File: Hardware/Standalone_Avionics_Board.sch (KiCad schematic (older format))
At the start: 4 parts, among them J1 GPS_Ant, J2 Charges Terminal Block, J3 RF_Ant, J6 3-Pin Molex Power

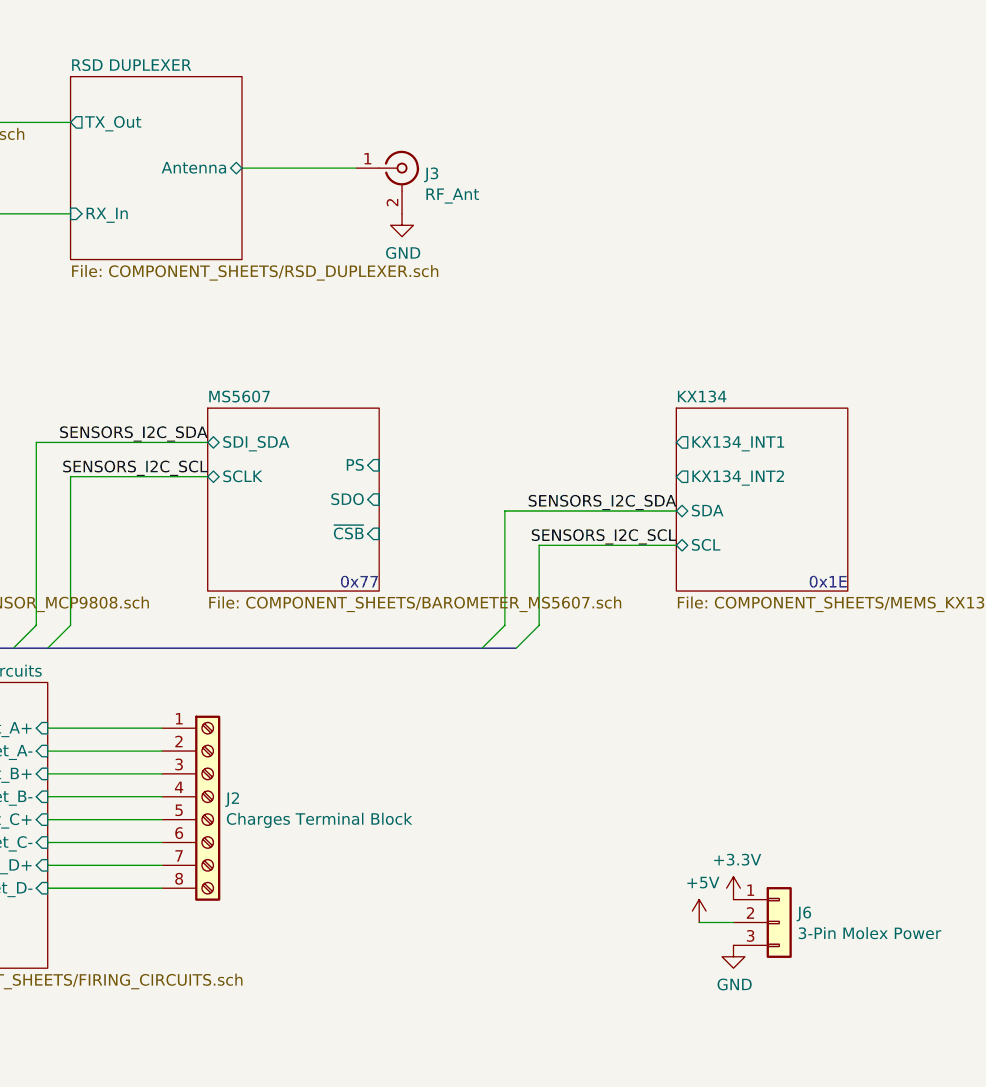
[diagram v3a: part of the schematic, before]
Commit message: Removed microcontroller clock to save space
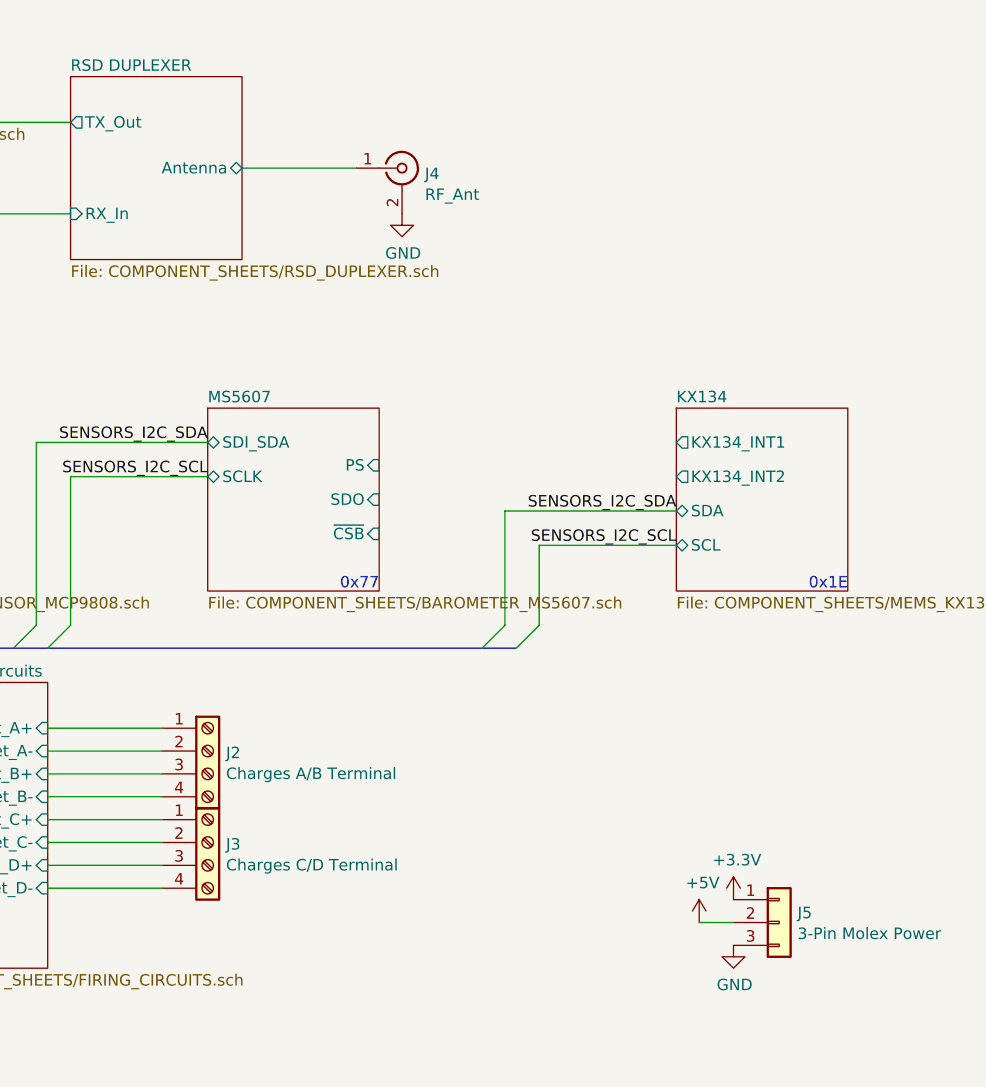
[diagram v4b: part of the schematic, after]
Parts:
- removed J2: Charges Terminal Block, TerminalBlock_Phoenix:TerminalBlock_Phoenix_MKDS-1,5-8-5.08_1x08_P5.08mm_Horizontal, symbol Connector:Screw_Terminal_01x08
- added J2: Charges A/B Terminal, TerminalBlock_Phoenix:TerminalBlock_Phoenix_MKDS-1,5-4_1x04_P5.00mm_Horizontal, symbol Connector:Screw_Terminal_01x04
- added J3: Charges C/D Terminal, TerminalBlock_Phoenix:TerminalBlock_Phoenix_MKDS-1,5-4_1x04_P5.00mm_Horizontal, symbol Connector:Screw_Terminal_01x04
- renumbered J3 to J4, J6 to J5
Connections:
- net Charges Firing Circuits/Fet_A+: now also J2.1 (Pin_1)
- net Charges Firing Circuits/Fet_A-: now also J2.2 (Pin_2)
- net Charges Firing Circuits/Fet_B+: now also J2.3 (Pin_3)
- net Charges Firing Circuits/Fet_B-: now also J2.4 (Pin_4)
- net Charges Firing Circuits/Fet_C+: now also J3.1 (Pin_1)
- net Charges Firing Circuits/Fet_C-: now also J3.2 (Pin_2)
- net Charges Firing Circuits/Fet_D+: now also J3.3 (Pin_3)
- net Charges Firing Circuits/Fet_D-: now also J3.4 (Pin_4)
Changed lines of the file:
@@
 $EndComp
 $Comp
-L Connector:Conn_Coaxial J3
+L Connector:Conn_Coaxial J4
 U 1 1 61B4987D
 P 8300 1700
-F 0 "J3" H 8400 1675 50  0000 L CNN
+F 0 "J4" H 8400 1675 50  0000 L CNN
 F 1 "RF_Ant" H 8400 1584 50  0000 L CNN
 F 2 "Connector_Coaxial:SMA_Amphenol_132134-11_Vertical" H 8300 1700 50  0001 C CNN
@@
 F5 "~CS" I L 3500 5350 50
 $EndSheet
-$Comp
-L Connector:Screw_Terminal_01x08 J2
-U 1 1 61EBDC84
-P 7450 4450
-F 0 "J2" H 7530 4442 50  0000 L CNN
-F 1 "Charges Terminal Block" H 7530 4351 50  0000 L CNN
-F 2 "TerminalBlock_Phoenix:TerminalBlock_Phoenix_MKDS-1,5-8-5.08_1x08_P5.08mm_Horizontal" H 7450 4450 50  0001 C CNN
-F 3 "~" H 7450 4450 50  0001 C CNN
-	1    7450 4450
-	1    0    0    -1
-$EndComp
 $Sheet
 S 5950 3950 800  1250
@@
 	7250 4850 6750 4850
 $Comp
-L power:+3.3V #PWR086
+L power:+3.3V #PWR04
 U 1 1 61B21EEA
 P 9750 4900
-F 0 "#PWR086" H 9750 4750 50  0001 C CNN
+F 0 "#PWR04" H 9750 4750 50  0001 C CNN
 F 1 "+3.3V" H 9765 5073 50  0000 C CNN
 F 2 "" H 9750 4900 50  0001 C CNN
@@
 $EndComp
 $Comp
-L power:GND #PWR087
+L power:GND #PWR05
 U 1 1 61B228F3
 P 9750 5100
-F 0 "#PWR087" H 9750 4850 50  0001 C CNN
+F 0 "#PWR05" H 9750 4850 50  0001 C CNN
 F 1 "GND" H 9755 4927 50  0000 C CNN
 F 2 "" H 9750 5100 50  0001 C CNN
@@
 $EndComp
 $Comp
-L Connector_Generic:Conn_01x03 J6
+L Connector_Generic:Conn_01x03 J5
 U 1 1 61B22E7C
 P 9950 5000
-F 0 "J6" H 10030 5042 50  0000 L CNN
+F 0 "J5" H 10030 5042 50  0000 L CNN
 F 1 "3-Pin Molex Power" H 10030 4951 50  0000 L CNN
 F 2 "Connector_Molex:Molex_KK-254_AE-6410-03A_1x03_P2.54mm_Vertical" H 9950 5000 50  0001 C CNN
@@
 $EndComp
 $Comp
-L power:+5V #PWR085
+L power:+5V #PWR03
 U 1 1 61B248E6
 P 9600 5000
-F 0 "#PWR085" H 9600 4850 50  0001 C CNN
+F 0 "#PWR03" H 9600 4850 50  0001 C CNN
 F 1 "+5V" H 9615 5173 50  0000 C CNN
 F 2 "" H 9600 5000 50  0001 C CNN
@@
 Wire Bus Line
 	2600 3800 8800 3800
+$Comp
+L Connector:Screw_Terminal_01x04 J2
+U 1 1 61B3C495
+P 7450 4250
+F 0 "J2" H 7530 4242 50  0000 L CNN
+F 1 "Charges A/B Terminal" H 7530 4151 50  0000 L CNN
+F 2 "TerminalBlock_Phoenix:TerminalBlock_Phoenix_MKDS-1,5-4_1x04_P5.00mm_Horizontal" H 7450 4250 50  0001 C CNN
+F 3 "~" H 7450 4250 50  0001 C CNN
+	1    7450 4250
+	1    0    0    -1
+$EndComp
+$Comp
+L Connector:Screw_Terminal_01x04 J3
+U 1 1 61B3D949
+P 7450 4650
+F 0 "J3" H 7530 4642 50  0000 L CNN
+F 1 "Charges C/D Terminal" H 7530 4551 50  0000 L CNN
+F 2 "TerminalBlock_Phoenix:TerminalBlock_Phoenix_MKDS-1,5-4_1x04_P5.00mm_Horizontal" H 7450 4650 50  0001 C CNN
+F 3 "~" H 7450 4650 50  0001 C CNN
+	1    7450 4650
+	1    0    0    -1
+$EndComp
 $EndSCHEMATC

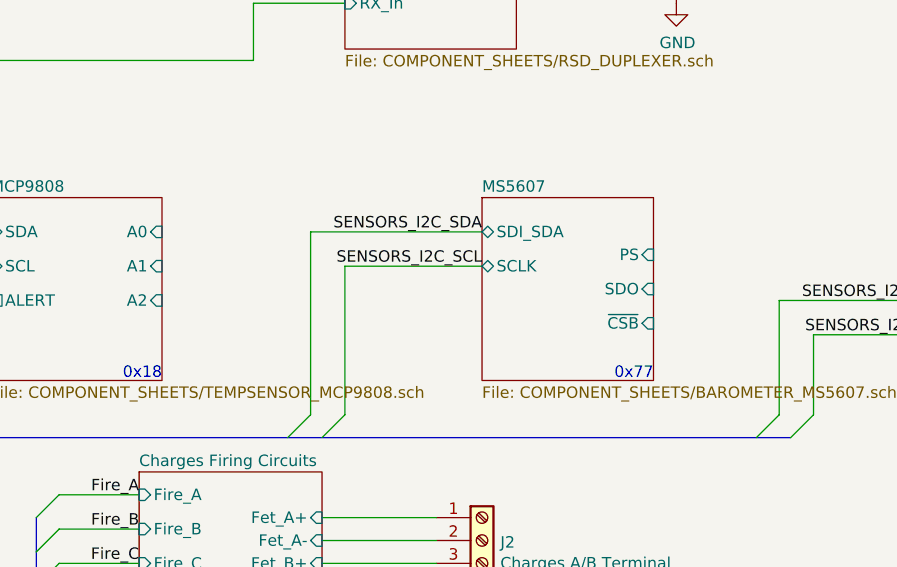
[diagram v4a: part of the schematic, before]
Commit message: Forced addresses for I2C devices
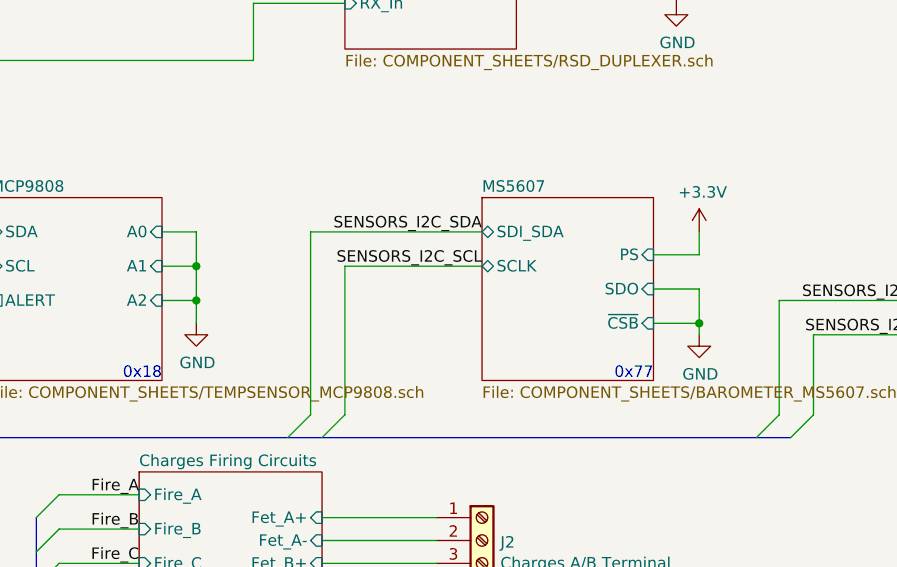
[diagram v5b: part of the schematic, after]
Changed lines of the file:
@@
 Wire Wire Line
 	9750 5000 9600 5000
-Wire Bus Line
-	2600 2900 2600 3800
-Wire Bus Line
-	2350 5850 2350 6500
-Wire Bus Line
-	2350 6500 2950 6500
-Wire Bus Line
-	2350 5500 3100 5500
-Wire Bus Line
-	2350 4850 2350 5500
-Wire Bus Line
-	2250 3500 2250 4550
-Wire Bus Line
-	5500 4150 5500 5200
-Wire Bus Line
-	2600 3800 8800 3800
 $Comp
 L Connector:Screw_Terminal_01x04 J2
@@
 	1    0    0    -1
 $EndComp
+$Comp
+L power:GND #PWR?
+U 1 1 61B8B67C
+P 6200 3300
+F 0 "#PWR?" H 6200 3050 50  0001 C CNN
+F 1 "GND" H 6205 3127 50  0000 C CNN
+F 2 "" H 6200 3300 50  0001 C CNN
+F 3 "" H 6200 3300 50  0001 C CNN
+	1    6200 3300
+	1    0    0    -1
+$EndComp
+Wire Wire Line
+	6200 3300 6200 3200
+Wire Wire Line
+	6200 2900 6050 2900
+Wire Wire Line
+	6050 3050 6200 3050
+Connection ~ 6200 3050
+Wire Wire Line
+	6200 3050 6200 2900
+Wire Wire Line
+	6050 3200 6200 3200
+Connection ~ 6200 3200
+Wire Wire Line
+	6200 3200 6200 3050
+$Comp
+L power:GND #PWR?
+U 1 1 61B9EF90
+P 8400 3350
+F 0 "#PWR?" H 8400 3100 50  0001 C CNN
+F 1 "GND" H 8405 3177 50  0000 C CNN
+F 2 "" H 8400 3350 50  0001 C CNN
+F 3 "" H 8400 3350 50  0001 C CNN
+	1    8400 3350
+	1    0    0    -1
+$EndComp
+Wire Wire Line
+	8400 3350 8400 3300
+Wire Wire Line
+	8400 3300 8200 3300
+Wire Wire Line
+	8200 3150 8400 3150
+Wire Wire Line
+	8400 3150 8400 3300
+Connection ~ 8400 3300
+$Comp
+L power:+3.3V #PWR?
+U 1 1 61BAA106
+P 8400 2900
+F 0 "#PWR?" H 8400 2750 50  0001 C CNN
+F 1 "+3.3V" H 8415 3073 50  0000 C CNN
+F 2 "" H 8400 2900 50  0001 C CNN
+F 3 "" H 8400 2900 50  0001 C CNN
+	1    8400 2900
+	1    0    0    -1
+$EndComp
+Wire Wire Line
+	8400 2900 8400 3000
+Wire Wire Line
+	8400 3000 8200 3000
+Wire Bus Line
+	2600 2900 2600 3800
+Wire Bus Line
+	2350 5850 2350 6500
+Wire Bus Line
+	2350 6500 2950 6500
+Wire Bus Line
+	2350 5500 3100 5500
+Wire Bus Line
+	2350 4850 2350 5500
+Wire Bus Line
+	2250 3500 2250 4550
+Wire Bus Line
+	5500 4150 5500 5200
+Wire Bus Line
+	2600 3800 8800 3800
 $EndSCHEMATC
